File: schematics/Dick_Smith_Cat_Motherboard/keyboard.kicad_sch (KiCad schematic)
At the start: 33 parts, among them J7 Keyboard, U37 74LS45, U41 74LS244, U44 8048

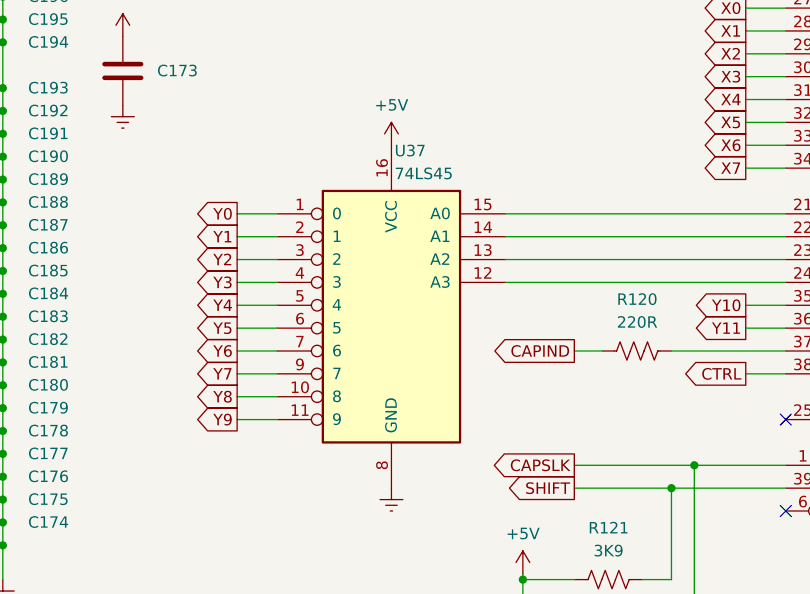
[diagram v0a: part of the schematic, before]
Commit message: Fix chip numbers in the motherboard schematic
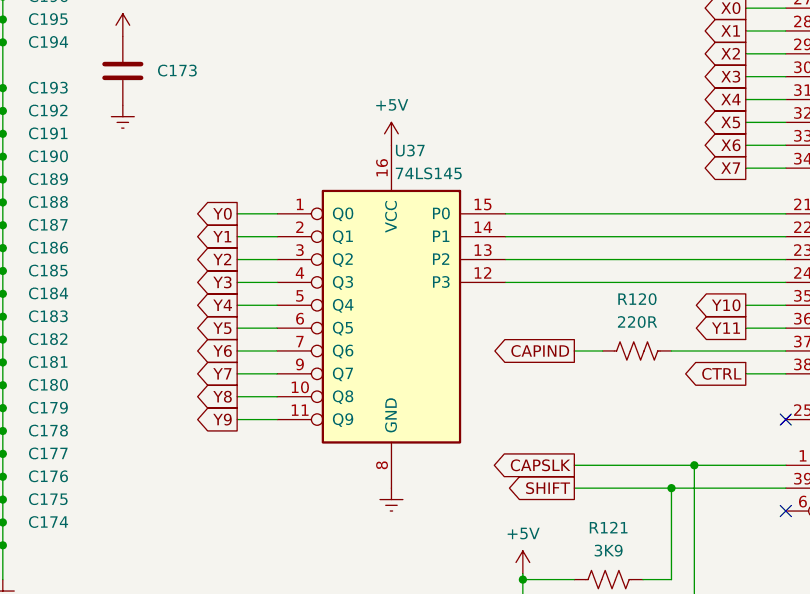
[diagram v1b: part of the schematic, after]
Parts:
- removed U37: 74LS45, Package_DIP:DIP-16_W7.62mm, symbol 74xx:74LS42
- added U37: 74LS145, Package_DIP:DIP-16_W7.62mm, symbol 74xx:74LS145
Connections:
- net +5V: now also U37.16 (VCC)
- net Earth: now also U37.8 (GND)
- net Y0: now also U37.1 (Q0)
- net Y1: now also U37.2 (Q1)
- net Y2: now also U37.3 (Q2)
- net Y3: now also U37.4 (Q3)
- net Y4: now also U37.5 (Q4)
- net Y5: now also U37.6 (Q5)
- net Y6: now also U37.7 (Q6)
- net Y7: now also U37.9 (Q7)
- net Y8: now also U37.10 (Q8)
- net Y9: now also U37.11 (Q9)
- net at U44.21 (P2.0): now also U37.15 (P0)
- net at U44.22 (P2.1): now also U37.14 (P1)
- net at U44.23 (P2.2): now also U37.13 (P2)
- net at U44.24 (P2.3): now also U37.12 (P3)
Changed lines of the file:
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@@
-    )
-  )
-  (symbol (lib_id "74xx:74LS42") (at 113.665 100.965 0) (mirror y) (unit 1)
-    (in_bom yes) (on_board yes) (dnp no) (fields_autoplaced)
-    (property "Reference" "U37" (at 114.0109 83.82 0)
-      (effects (font (size 1.27 1.27)) (justify right))
-    )
-    (property "Value" "74LS45" (at 114.0109 86.36 0)
-      (effects (font (size 1.27 1.27)) (justify right))
-    )
-    (property "Footprint" "Package_DIP:DIP-16_W7.62mm" (at 113.665 100.965 0)
-      (effects (font (size 1.27 1.27)) hide)
-    )
-    (property "Datasheet" "http://www.ti.com/lit/gpn/sn74LS42" (at 113.665 100.965 0)
-      (effects (font (size 1.27 1.27)) hide)
-    )
-    (pin "8")
-    (pin "16")
-    (pin "14")
-    (pin "11")
-    (pin "15")
-    (pin "9")
-    (pin "7")
-    (pin "12")
-    (pin "2")
-    (pin "4")
-    (pin "5")
-    (pin "6")
-    (pin "3")
-    (pin "10")
-    (pin "1")
-    (pin "13")
-    (instances
-      (project "Dick_Smith_Cat_Motherboard"
-        (path "/b825002a-fcdd-4970-89c6-1645cf48180b/f8bc6f98-3283-43e9-be9b-076d2e56931b"
-          (reference "U37") (unit 1)
-        )
-      )
     )
   )
@@
         )
       )
+    )
+  )
+  (symbol (lib_id "74xx:74LS145") (at 113.665 100.965 0) (mirror y) (unit 1)
+    (in_bom yes) (on_board yes) (dnp no) (fields_autoplaced)
+    (property "Reference" "U37" (at 114.0109 83.82 0)
+      (effects (font (size 1.27 1.27)) (justify right))
+    )
+    (property "Value" "74LS145" (at 114.0109 86.36 0)
+      (effects (font (size 1.27 1.27)) (justify right))
+    )
+    (property "Footprint" "Package_DIP:DIP-16_W7.62mm" (at 113.665 100.965 0)
+      (effects (font (size 1.27 1.27)) hide)
+    )
+    (property "Datasheet" "http://www.ti.com/lit/gpn/sn74LS145" (at 113.665 100.965 0)
+      (effects (font (size 1.27 1.27)) hide)
+    )
+    (pin "5")
+    (pin "3")
+    (pin "7")
+    (pin "6")
+    (pin "1")
+    (pin "9")
+    (pin "2")
+    (pin "8")
+    (pin "16")
+    (pin "4")
+    (pin "14")
+    (pin "10")
+    (pin "13")
+    (pin "12")
+    (pin "11")
+    (pin "15")
+    (instances
+      (project "Dick_Smith_Cat_Motherboard"
+        (path "/b825002a-fcdd-4970-89c6-1645cf48180b/f8bc6f98-3283-43e9-be9b-076d2e56931b"
+          (reference "U37") (unit 1)
+        )
+      )
